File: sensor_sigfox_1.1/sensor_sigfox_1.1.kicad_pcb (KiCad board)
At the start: 2 copper layers, 27.8 x 60.1 mm, 19 parts, among them IC1 WSSFM11R2DAT, J1 Battery, J2 Conn_01x07_Socket, J3 Conn_01x01_Female, J4 Antenna, U1 ATtiny826-X, U2 MLX90393, Y1 32.768 kHz

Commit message: revision 1.1.1
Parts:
- removed R1: 470, Resistor_SMD:R_0805_2012Metric_Pad1.20x1.40mm_HandSolder
- moved Y1 7.46 mm to (133.0, 76.2)
- moved C1 7.32 mm to (124.7, 74.2)
- moved U1 7.26 mm to (128.7, 74.3)
- moved C2 7.20 mm to (122.8, 74.2)
- moved C4 6.36 mm to (136.3, 72.6), turned to 180 degrees
- moved C3 4.19 mm to (136.4, 77.4)
- moved C6 3.29 mm to (119.7, 90.6), turned to -90 degrees
- moved J3 2.84 mm to (137.5, 93.4)
- moved IC1 2.30 mm to (130.9, 85.6)
- moved R2 1.50 mm to (137.8, 54.4), turned to 180 degrees
- moved R3 1.44 mm to (137.9, 52.4), turned to 180 degrees
- moved J4 1.02 mm to (134.0, 94.1)
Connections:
- C5 pad 2: Net-(U1-PC3) -> VCC
- U1 pad 18: Net-(U1-PC3) -> unconnected-(U1-PC3-Pad18)
- U1 pad 19: Net-(U1-~{RESET}/PA0) -> Net-(J2-Pin_3)
- U2 pad 10: GND -> unconnected-(U2-N/C-Pad10)
- U2 pad 11: unconnected-(U2-A1-Pad11) -> VCC
- U2 pad 12: unconnected-(U2-A0-Pad12) -> VCC
- U2 pad 14: GND -> unconnected-(U2-N/C-Pad14)
- U2 pad 15: Net-(U1-PC3) -> VCC
- U2 pad 16: GND -> unconnected-(U2-N/C-Pad16)
- U2 pad 2: unconnected-(U2-MS/CS-Pad2) -> VCC
- U2 pad 8: Net-(U1-PC3) -> VCC
- U2 pad 9: GND -> unconnected-(U2-N/C-Pad9)
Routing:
- net Net-(U1-PC3): track 46.1 -> 0.00 mm
- net Net-(U1-~{RESET}/PA0): track 37.0 -> 0.00 mm
- net Net-(J2-Pin_3): track 2.94 -> 37.3 mm, vias 0 -> 1
- net GND: track 172.3 -> 147.4 mm, vias 6 -> 1
- net VCC: track 125.1 -> 114.7 mm, vias 3 -> 2
- net Net-(IC1-GPIO4): track 45.1 -> 51.0 mm, vias 4 -> 2
- net Net-(IC1-RF_IO): track 10.0 -> 5.47 mm
- net /SDA: track 79.1 -> 80.7 mm
- net Net-(U1-PB3): track 5.20 -> 6.18 mm
- net Net-(U1-PB2): track 5.16 -> 5.94 mm
- net Net-(IC1-RST_N): track 23.4 -> 22.6 mm, vias 0 -> 2
- net /SCL: track 78.3 -> 77.6 mm, vias 1 -> 3
- net /SF_RX: track 43.4 -> 44.0 mm, vias 1 -> 3
- net /SF_TX: track 43.6 -> 44.0 mm, vias 1 -> 3

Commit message: pcb 1.1
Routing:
- net GND: track 147.4 -> 197.0 mm, vias 1 -> 2
- net Net-(U1-PB2): track 5.94 -> 6.65 mm
- net VCC: track 114.7 -> 114.1 mm
- net Net-(IC1-RST_N): track 22.6 -> 22.0 mm

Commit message: gerber y conexiones int/trig
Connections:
- U1 pad 2: unconnected-(U1-PA3-Pad2) -> Net-(U1-PA3)
- U1 pad 5: unconnected-(U1-PA4-Pad5) -> Net-(U1-PA4)
- U2 pad 1: unconnected-(U2-INT-Pad1) -> Net-(U1-PA3)
- U2 pad 4: GND -> unconnected-(U2-N/C-Pad4)
- U2 pad 7: unconnected-(U2-INT/TRIG-Pad7) -> Net-(U1-PA4)
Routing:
- net Net-(U1-PA4): track 0.00 -> 68.5 mm, vias 0 -> 2
- net Net-(U1-PA3): track 0.00 -> 51.9 mm, vias 0 -> 2
- net GND: track 197.0 -> 196.4 mm
- net Net-(IC1-GPIO4): track 51.0 -> 50.5 mm

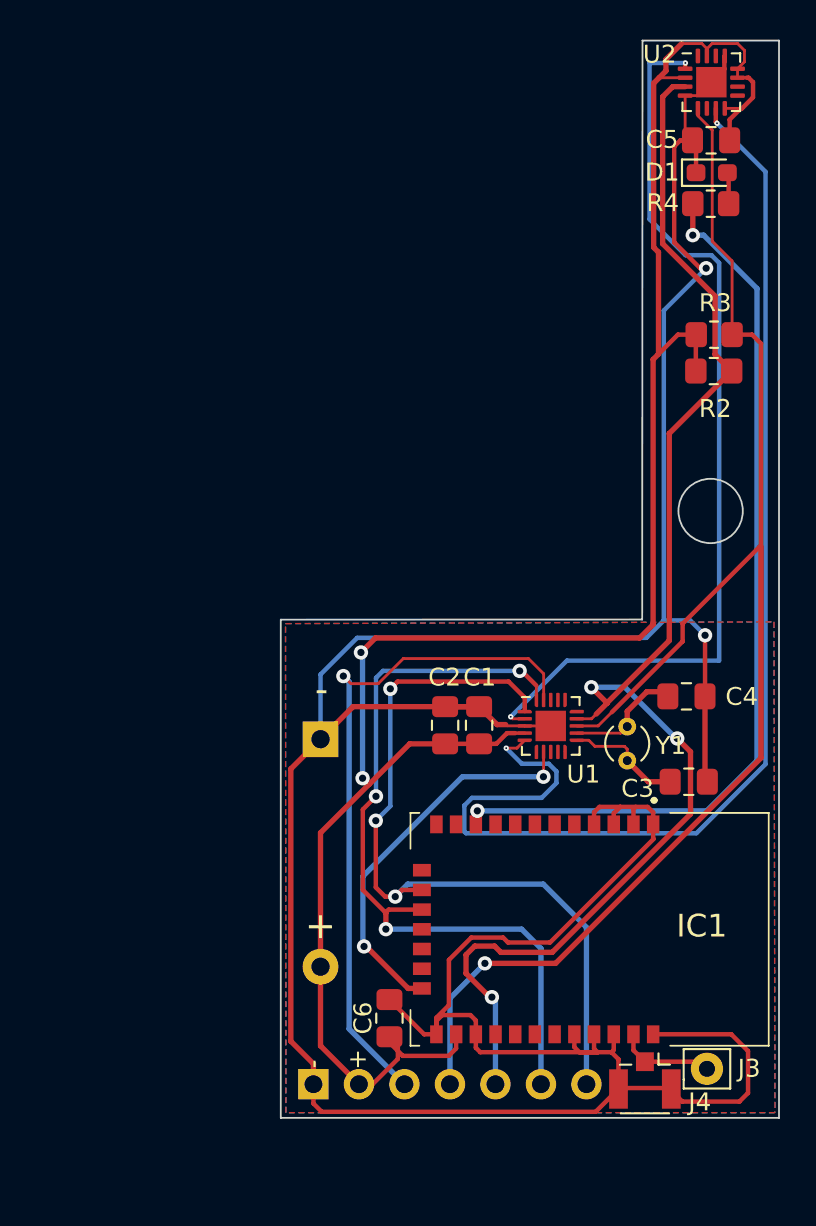
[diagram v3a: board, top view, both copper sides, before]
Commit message: 1.1 y 1.2 actualizados
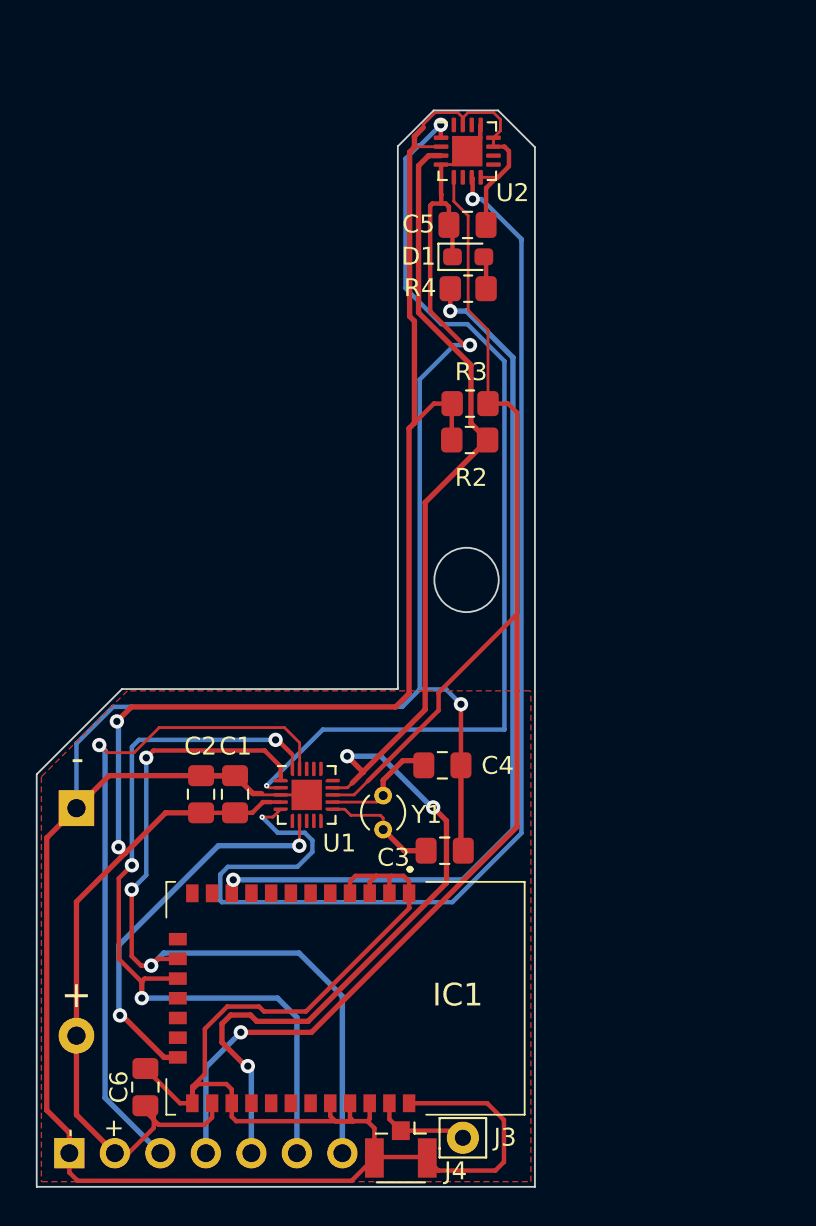
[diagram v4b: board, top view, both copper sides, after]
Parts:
- moved C5 14.4 mm to (124.1, 46.3)
- moved D1 14.4 mm to (124.1, 48.1)
- moved R4 14.3 mm to (124.1, 49.9)
- moved C4 14.2 mm to (122.7, 76.5)
- moved U1 14.2 mm to (115.1, 78.1)
- moved R2 14.2 mm to (124.2, 58.3)
- moved C1 14.2 mm to (111.1, 78.1)
- moved C6 14.2 mm to (106.1, 94.4)
- moved R3 14.2 mm to (124.2, 56.3)
- moved C2 14.2 mm to (109.2, 78.1)
- moved J1 14.2 mm to (102.3, 78.9)
- moved J2 14.2 mm to (101.9, 98.1)
- moved J4 14.2 mm to (120.4, 97.9)
- moved Y1 14.2 mm to (119.4, 80.0)
- moved U2 14.2 mm to (124.1, 42.2)
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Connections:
- U2 pad 4: unconnected-(U2-N/C-Pad4) -> GND
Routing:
- net Net-(U1-PA3): track 51.9 -> 54.2 mm
- net GND: track 196.4 -> 198.3 mm
- net VCC: track 114.1 -> 115.1 mm
- net Net-(IC1-GPIO4): track 50.5 -> 49.9 mm
- removed copper zone on B.Cu, net GND
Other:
- outline, holes or cut-outs redrawn
